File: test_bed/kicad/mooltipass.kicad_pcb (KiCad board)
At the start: 2 copper layers, 14 parts, among them CON1 AVR-ISP-6, P1 CONN_8, P2 CONN_6, P3 CONN_10, P4 CONN_8, P5 CONN_1, P6 CONN_1, P7 CONN_1, P8 CONN_1

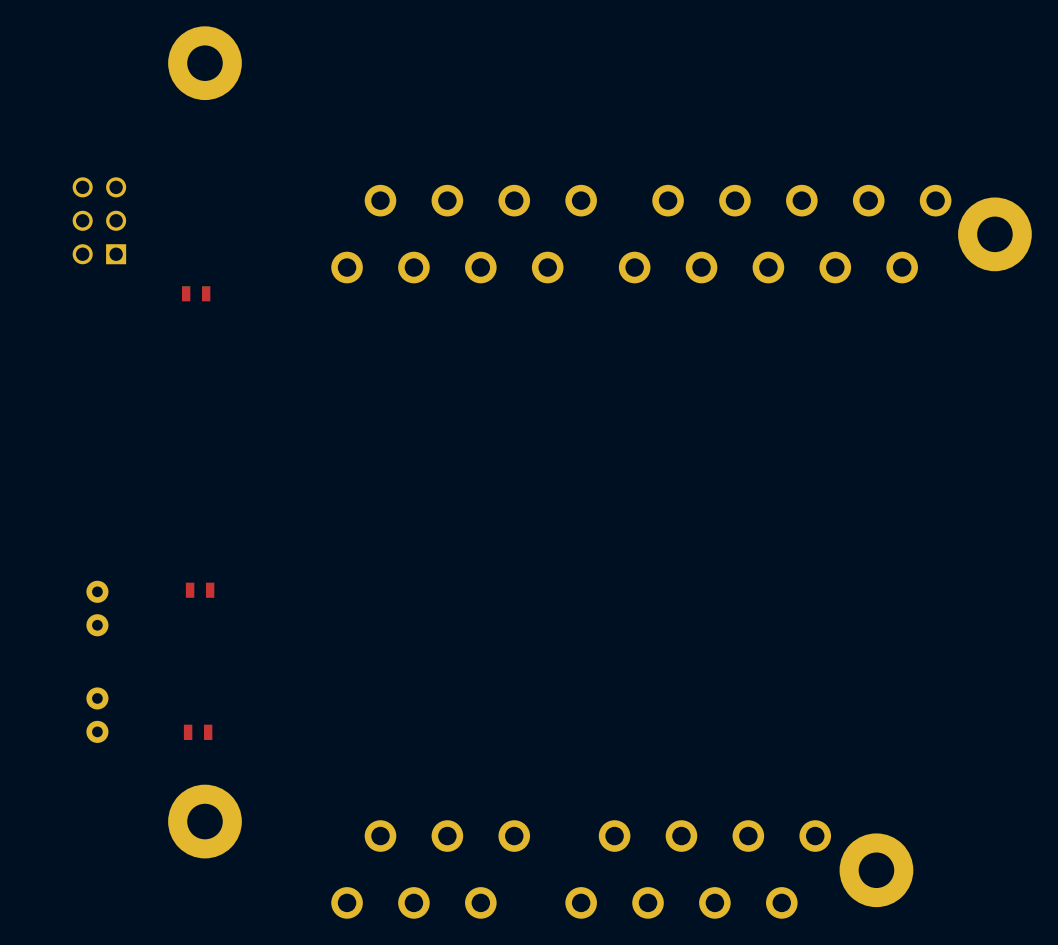
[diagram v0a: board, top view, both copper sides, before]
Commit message: mooltipass electrical test bed complete
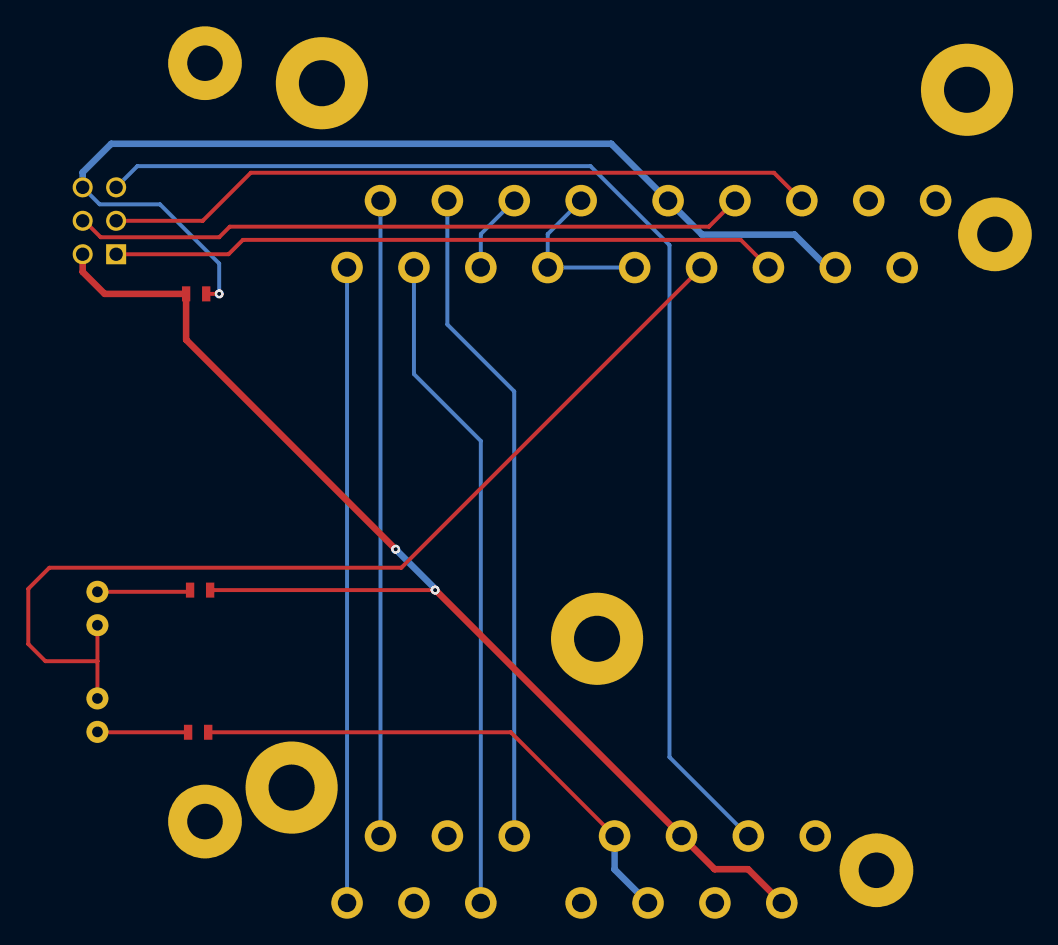
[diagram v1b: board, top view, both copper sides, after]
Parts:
- added P10: CONN_1, HOLE_FIX_M3, F.Cu at (119.0, 73.3)
- added P11: CONN_1, HOLE_FIX_M3, F.Cu at (139.9, 115.5)
- added P12: CONN_1, HOLE_FIX_M3, F.Cu at (116.7, 126.8)
- added P9: CONN_1, HOLE_FIX_M3, F.Cu at (168.0, 73.8)
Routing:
- net GND: track 0.00 -> 119.4 mm, vias 0 -> 1
- net +5V: track 0.00 -> 93.5 mm, vias 0 -> 2
- net /nRESET: track 0.00 -> 92.5 mm
- net /PB6: track 0.00 -> 76.8 mm
- net /SPI_SCK: track 0.00 -> 54.5 mm
- net /SPI_MOSI: track 0.00 -> 51.2 mm
- net /SPI_MISO: track 0.00 -> 50.9 mm
- net /I2C_SDA: track 0.00 -> 50.4 mm
- net /I2C_SCL: track 0.00 -> 50.4 mm
- net /PD2: track 0.00 -> 48.3 mm
- net /PD3: track 0.00 -> 48.3 mm
- net /PB4: track 0.00 -> 12.7 mm
- net N-000002: track 0.00 -> 7.09 mm
- net N-000003: track 0.00 -> 6.90 mm
- net /PC6: track 0.00 -> 6.13 mm
